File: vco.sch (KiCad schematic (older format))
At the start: 6 parts

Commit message: Schematic finished
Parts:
- gave numbers to parts that had none: 6
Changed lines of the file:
@@
 LIBS:2450bl15b050
 LIBS:tlv4172
+LIBS:l4940d2t12-tr
+LIBS:tps54308
+LIBS:l78l33abu
+LIBS:adp150aujz-18
 LIBS:radar-cache
+LIBS:hn1c01fu
 EELAYER 25 0
 EELAYER END
 $Descr A4 11693 8268
 encoding utf-8
-Sheet 2 7
+Sheet 2 8
 Title ""
 Date ""
@@
 $EndDescr
 $Comp
-L MAX2750 U?
+L MAX2750 U201
 U 1 1 59D5427A
 P 5090 3570
-F 0 "U?" H 5090 3570 60  0000 C CNN
+F 0 "U201" H 5090 3570 60  0000 C CNN
 F 1 "MAX2750" H 5340 3020 60  0000 C CNN
 F 2 "" H 5090 3570 60  0001 C CNN
@@
 $EndComp
 $Comp
-L C_Small C?
+L C_Small C203
 U 1 1 59D54372
 P 6720 3370
-F 0 "C?" H 6730 3440 50  0000 L CNN
+F 0 "C203" H 6730 3440 50  0000 L CNN
 F 1 "220u" H 6730 3290 50  0000 L CNN
 F 2 "" H 6720 3370 50  0001 C CNN
@@
 $EndComp
 $Comp
-L C_Small C?
+L C_Small C202
 U 1 1 59D543D5
 P 7000 3360
-F 0 "C?" H 7010 3430 50  0000 L CNN
+F 0 "C202" H 7010 3430 50  0000 L CNN
 F 1 "220u" H 7010 3280 50  0000 L CNN
 F 2 "" H 7000 3360 50  0001 C CNN
@@
 Connection ~ 6720 3220
 $Comp
-L GND #PWR?
+L GND #PWR025
 U 1 1 59D5445A
 P 6870 3770
-F 0 "#PWR?" H 6870 3520 50  0001 C CNN
+F 0 "#PWR025" H 6870 3520 50  0001 C CNN
 F 1 "GND" H 6870 3620 50  0000 C CNN
 F 2 "" H 6870 3770 50  0001 C CNN
@@
 Connection ~ 6870 3550
 $Comp
-L GND #PWR?
+L GND #PWR026
 U 1 1 59D54491
 P 4890 4380
-F 0 "#PWR?" H 4890 4130 50  0001 C CNN
+F 0 "#PWR026" H 4890 4130 50  0001 C CNN
 F 1 "GND" H 4890 4230 50  0000 C CNN
 F 2 "" H 4890 4380 50  0001 C CNN
@@
 Connection ~ 5830 3220
 $Comp
-L taper T?
+L taper T201
 U 1 1 59D5492A
 P 6110 3670
-F 0 "T?" H 6090 3800 60  0000 C CNN
+F 0 "T201" H 6090 3800 60  0000 C CNN
 F 1 "taper" H 6010 3540 60  0000 C CNN
 F 2 "" H 6110 3670 60  0001 C CNN
@@
 	6410 3670 6560 3670
 $Comp
-L C_Small C?
+L C_Small C201
 U 1 1 59D54B4D
 P 3650 3350
-F 0 "C?" H 3660 3420 50  0000 L CNN
+F 0 "C201" H 3660 3420 50  0000 L CNN
 F 1 "0u1" H 3660 3270 50  0000 L CNN
 F 2 "" H 3650 3350 50  0001 C CNN
@@
 $EndComp
 $Comp
-L GND #PWR?
+L GND #PWR027
 U 1 1 59D54C55
 P 3650 3540
-F 0 "#PWR?" H 3650 3290 50  0001 C CNN
+F 0 "#PWR027" H 3650 3290 50  0001 C CNN
 F 1 "GND" H 3650 3390 50  0000 C CNN
 F 2 "" H 3650 3540 50  0001 C CNN
@@
 	4190 3420 4440 3420
 $Comp
-L +3V3 #PWR?
+L +3V3 #PWR028
 U 1 1 59D54D8A
 P 5830 3110
-F 0 "#PWR?" H 5830 2960 50  0001 C CNN
+F 0 "#PWR028" H 5830 2960 50  0001 C CNN
 F 1 "+3V3" H 5830 3250 50  0000 C CNN
 F 2 "" H 5830 3110 50  0001 C CNN
@@
 $EndComp
 $Comp
-L +3V3 #PWR?
+L +3V3 #PWR029
 U 1 1 59D54DAB
 P 4310 2840
-F 0 "#PWR?" H 4310 2690 50  0001 C CNN
+F 0 "#PWR029" H 4310 2690 50  0001 C CNN
 F 1 "+3V3" H 4310 2980 50  0000 C CNN
 F 2 "" H 4310 2840 50  0001 C CNN
@@
 $EndComp
 $Comp
-L R_Small R?
+L R_Small R201
 U 1 1 59D54DC2
 P 4310 2990
-F 0 "R?" H 4340 3010 50  0000 L CNN
+F 0 "R201" H 4340 3010 50  0000 L CNN
 F 1 "10k" H 4340 2950 50  0000 L CNN
 F 2 "" H 4310 2990 50  0001 C CNN

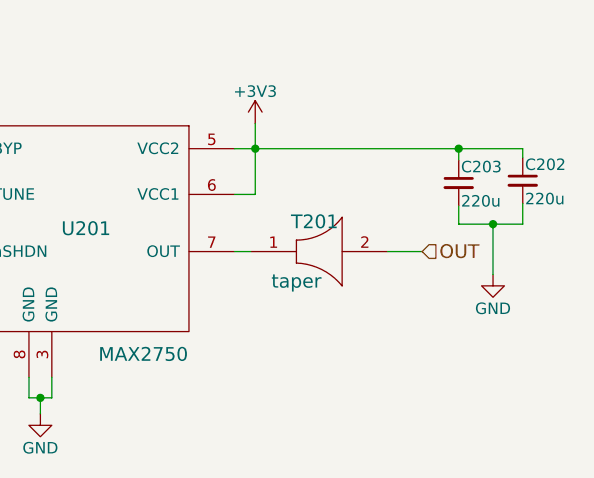
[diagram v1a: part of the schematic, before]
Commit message: Assign a lot of footprints, fix l78l33abu part (input and output were reversed)
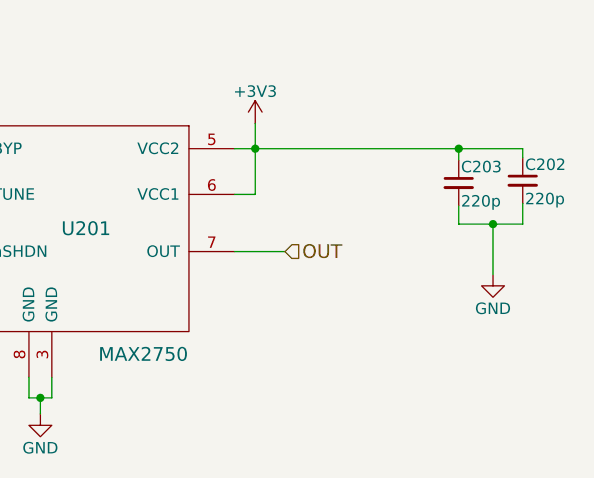
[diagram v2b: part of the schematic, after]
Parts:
- removed T201: taper, symbol taper
- C201: footprint (none) -> Capacitors_SMD:C_0603_HandSoldering
- C202, C203: value 220u -> 220p; footprint (none) -> Capacitors_SMD:C_0402
- R201: footprint (none) -> Resistors_SMD:R_0603_HandSoldering
- U201: footprint (none) -> rajsradar:U8+1
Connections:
- net OUT: now also U201.7 (OUT)
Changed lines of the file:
@@
 F 0 "U201" H 5090 3570 60  0000 C CNN
 F 1 "MAX2750" H 5340 3020 60  0000 C CNN
-F 2 "" H 5090 3570 60  0001 C CNN
+F 2 "rajsradar:U8+1" H 5090 3570 60  0001 C CNN
 F 3 "" H 5090 3570 60  0001 C CNN
 	1    5090 3570
@@
 P 6720 3370
 F 0 "C203" H 6730 3440 50  0000 L CNN
-F 1 "220u" H 6730 3290 50  0000 L CNN
-F 2 "" H 6720 3370 50  0001 C CNN
+F 1 "220p" H 6730 3290 50  0000 L CNN
+F 2 "Capacitors_SMD:C_0402" H 6720 3370 50  0001 C CNN
 F 3 "" H 6720 3370 50  0001 C CNN
 	1    6720 3370
@@
 P 7000 3360
 F 0 "C202" H 7010 3430 50  0000 L CNN
-F 1 "220u" H 7010 3280 50  0000 L CNN
-F 2 "" H 7000 3360 50  0001 C CNN
+F 1 "220p" H 7010 3280 50  0000 L CNN
+F 2 "Capacitors_SMD:C_0402" H 7000 3360 50  0001 C CNN
 F 3 "" H 7000 3360 50  0001 C CNN
 	1    7000 3360
@@
 Connection ~ 6720 3220
 $Comp
-L GND #PWR025
+L GND #PWR026
 U 1 1 59D5445A
 P 6870 3770
-F 0 "#PWR025" H 6870 3520 50  0001 C CNN
+F 0 "#PWR026" H 6870 3520 50  0001 C CNN
 F 1 "GND" H 6870 3620 50  0000 C CNN
 F 2 "" H 6870 3770 50  0001 C CNN
@@
 Connection ~ 6870 3550
 $Comp
-L GND #PWR026
+L GND #PWR027
 U 1 1 59D54491
 P 4890 4380
-F 0 "#PWR026" H 4890 4130 50  0001 C CNN
+F 0 "#PWR027" H 4890 4130 50  0001 C CNN
 F 1 "GND" H 4890 4230 50  0000 C CNN
 F 2 "" H 4890 4380 50  0001 C CNN
@@
 	4890 4380 4890 4310
 Connection ~ 4890 4310
-Text HLabel 6560 3670 2    60   Input ~ 0
+Text HLabel 5960 3670 2    60   Input ~ 0
 OUT
 Connection ~ 5830 3220
-$Comp
-L taper T201
-U 1 1 59D5492A
-P 6110 3670
-F 0 "T201" H 6090 3800 60  0000 C CNN
-F 1 "taper" H 6010 3540 60  0000 C CNN
-F 2 "" H 6110 3670 60  0001 C CNN
-F 3 "" H 6110 3670 60  0001 C CNN
-	1    6110 3670
-	1    0    0    -1
-$EndComp
 Wire Wire Line
-	5740 3670 5810 3670
-Wire Wire Line
-	6410 3670 6560 3670
+	5740 3670 5960 3670
 $Comp
 L C_Small C201
@@
 F 0 "C201" H 3660 3420 50  0000 L CNN
 F 1 "0u1" H 3660 3270 50  0000 L CNN
-F 2 "" H 3650 3350 50  0001 C CNN
+F 2 "Capacitors_SMD:C_0603_HandSoldering" H 3650 3350 50  0001 C CNN
 F 3 "" H 3650 3350 50  0001 C CNN
 	1    3650 3350
@@
 $EndComp
 $Comp
-L GND #PWR027
+L GND #PWR028
 U 1 1 59D54C55
 P 3650 3540
-F 0 "#PWR027" H 3650 3290 50  0001 C CNN
+F 0 "#PWR028" H 3650 3290 50  0001 C CNN
 F 1 "GND" H 3650 3390 50  0000 C CNN
 F 2 "" H 3650 3540 50  0001 C CNN
@@
 	4190 3420 4440 3420
 $Comp
-L +3V3 #PWR028
+L +3V3 #PWR029
 U 1 1 59D54D8A
 P 5830 3110
-F 0 "#PWR028" H 5830 2960 50  0001 C CNN
+F 0 "#PWR029" H 5830 2960 50  0001 C CNN
 F 1 "+3V3" H 5830 3250 50  0000 C CNN
 F 2 "" H 5830 3110 50  0001 C CNN
@@
 $EndComp
 $Comp
-L +3V3 #PWR029
+L +3V3 #PWR030
 U 1 1 59D54DAB
 P 4310 2840
-F 0 "#PWR029" H 4310 2690 50  0001 C CNN
+F 0 "#PWR030" H 4310 2690 50  0001 C CNN
 F 1 "+3V3" H 4310 2980 50  0000 C CNN
 F 2 "" H 4310 2840 50  0001 C CNN
@@
 F 0 "R201" H 4340 3010 50  0000 L CNN
 F 1 "10k" H 4340 2950 50  0000 L CNN
-F 2 "" H 4310 2990 50  0001 C CNN
+F 2 "Resistors_SMD:R_0603_HandSoldering" H 4310 2990 50  0001 C CNN
 F 3 "" H 4310 2990 50  0001 C CNN
 	1    4310 2990

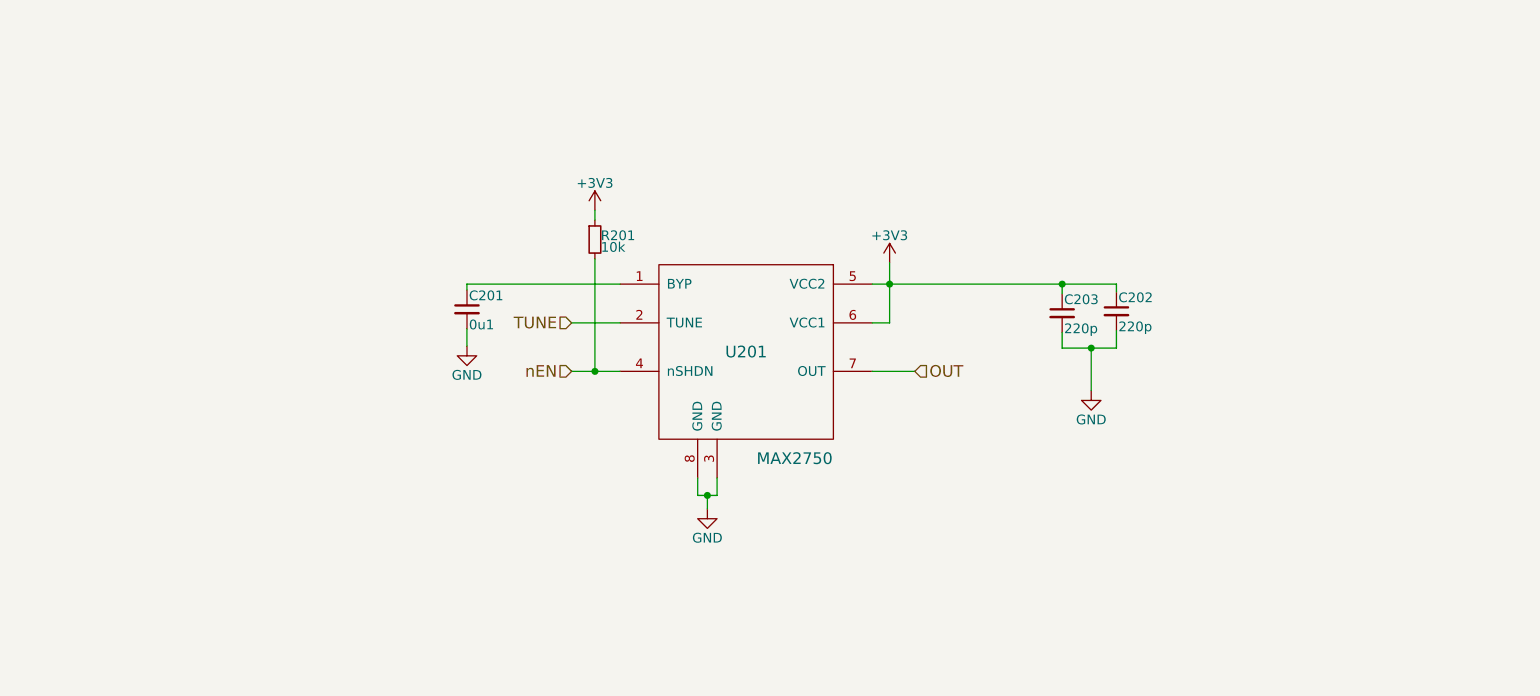
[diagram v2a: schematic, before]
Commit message: Finished circuit layout (for the RF board)
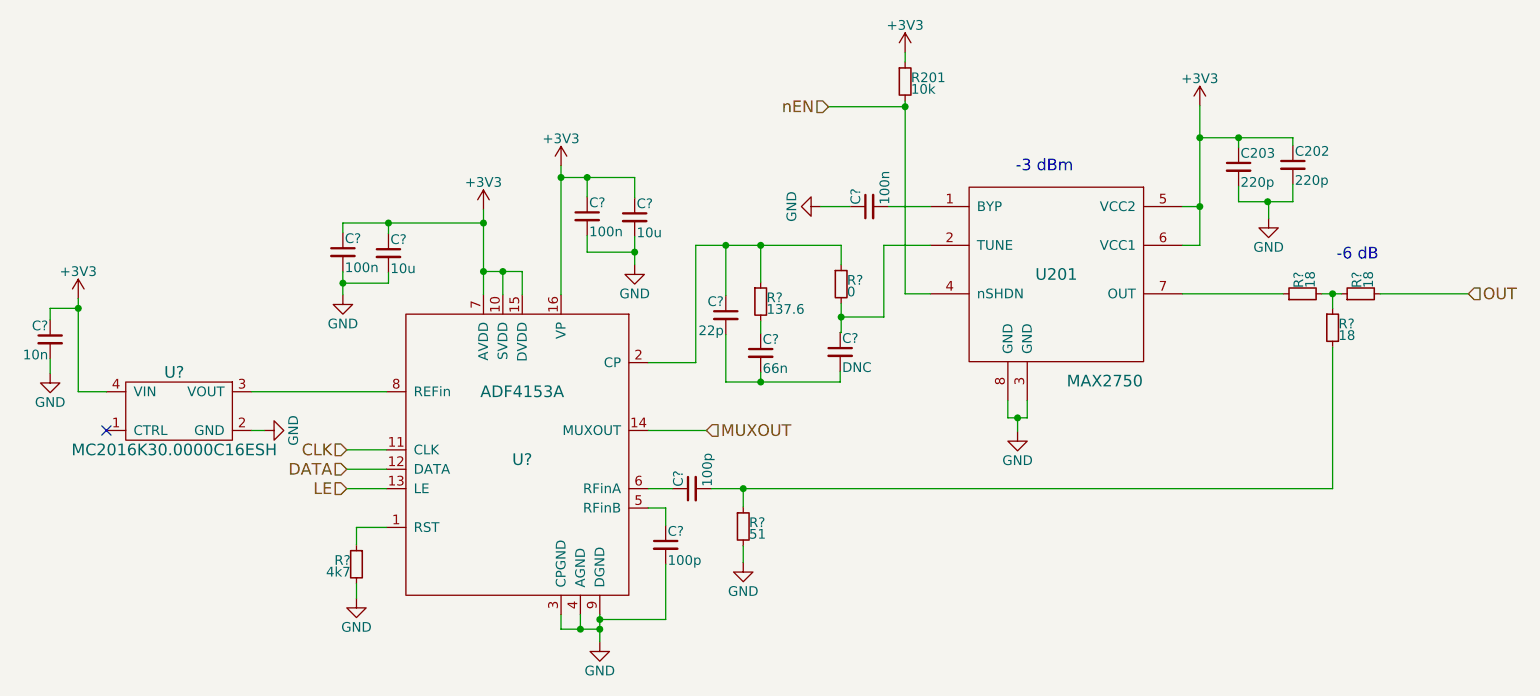
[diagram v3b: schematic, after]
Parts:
- removed C201: 0u1, Capacitors_SMD:C_0603_HandSoldering, symbol C_Small
- added C? (x2): 100p, symbol C_Small
- added C?: 66n, symbol C_Small
- added C?: 22p, symbol C_Small
- added C?: DNC, symbol C_Small
- added C? (x3): 100n, symbol C_Small
- added C? (x2): 10u, symbol C_Small
- added C?: 10n, symbol C_Small
- added R? (x3): 18, symbol R_Small
- added R?: 51, symbol R_Small
- added R?: 137.6, symbol R_Small
- added R?: 0, symbol R_Small
- added R?: 4k7, symbol R_Small
- added U?: ADF4153A, symbol ADF4153A
- added U?: MC2016K30.0000C16ESH, symbol MC2016K30.0000C16ESH
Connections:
- net +3V3: now also C?.1, C?.1, C?.1, C?.1, C?.1, U?.10 (SVDD), U?.15 (DVDD), U?.16 (VP), U?.4 (VIN), U?.7 (AVDD)
- net GND: now also C?.1, C?.2, C?.2, C?.2, C?.2, C?.2, C?.2, R?.2, R?.2, U?.2 (GND), U?.3 (CPGND), U?.4 (AGND), U?.9 (DGND); no longer C202.2, C203.2
- net OUT: now also R?.2; no longer U201.7 (OUT)
- net at U201.1 (BYP): now also C?.2
- net TUNE: no longer names the net of U201.2 (TUNE)
- net TUNE: now also C?.1, R?.2
- new net: R?.1, U201.7 (OUT)
- new net: C202.2, C203.2
- new net: R?.1, U?.1 (RST)
- new net: C?.1, R?.1, R?.1, U?.2 (CP)
- new net: C?.1, U?.5 (RFinB)
- new net: C?.1, U?.6 (RFinA)
- new net: U?.3 (VOUT), U?.8 (REFin)
- new net: R?.1, R?.1, R?.2
- new net: C?.2, R?.1, R?.2
- new net: C?.1, R?.2
- new net: C?.2, C?.2, C?.2
- new net CLK: U?.11 (CLK)
- new net DATA: U?.12 (DATA)
- new net LE: U?.13 (LE)
- new net MUXOUT: U?.14 (MUXOUT)
- no-connect marks 0 -> 1
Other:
- note added: "-3 dBm"
- note added: "-6 dB"
- moved on the sheet: C202, C203, R201, U201
